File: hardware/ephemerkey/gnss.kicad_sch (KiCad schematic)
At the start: 12 parts

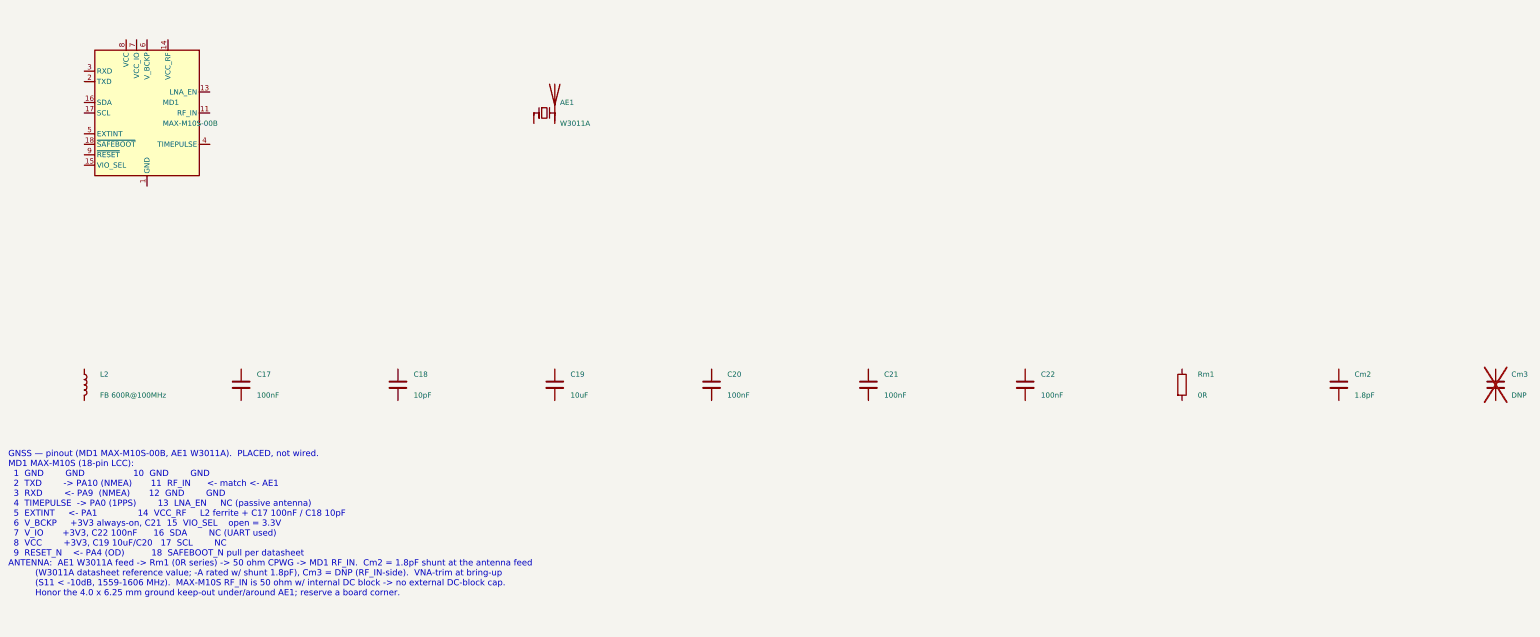
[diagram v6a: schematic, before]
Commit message: hardware: fix PSU load-share S/D, make all sheet notes monospace
The PSU wiring note specified Q1 (AO3401A load-share PMOS) as S=BAT+,
D=VSYS. A PMOS body diode conducts D->S, so that orientation points the
diode VSYS -> BAT+: with USB attached VSYS sits ~4.7V (VBUS - D3) against
a 3.0-4.2V cell, forward-biasing it and dumping uncontrolled current into
the battery, bypassing the MCP73831 charger entirely.

Correct assignment is D=BAT+, S=VSYS, so the body diode points BAT+ ->
VSYS: the battery always reaches the load, and USB can never back-feed
the cell. Q1 was placed but never wired (all three pins are unconnected
in the netlist), so this is a spec fix ahead of wiring, not a board
change. The lock's Q3 is a high-side switch and deliberately uses the
opposite S/D assignment; the note now says so, to stop the two being
"reconciled" by pattern-matching.

Also relaid the PSU note as a two-column table and gave every sheet note
the Courier New face the generator already emits (kschgen NOTE_FONT, added
in 43a6067). The sheets predate that commit, so their notes rendered in
KiCad's variable-width stroke font and the space-padded pin tables did not
line up. Font only on the other six notes -- text is untouched.

Verified: kicad-cli netlists for both boards are byte-identical before and
after (ephemerkey 259 nodes, lock 131 nodes) once the export timestamp is
excluded; no non-font lines changed in any sheet; all sheets re-rendered
and the notes fit inside the page frame.

The four ephemerkey sheets also carry pre-existing eeschema reformatting
(expanded lib_symbols) that was already in the working tree.

Co-Authored-By: Claude Opus 4.8 (1M context) <noreply@anthropic.com>
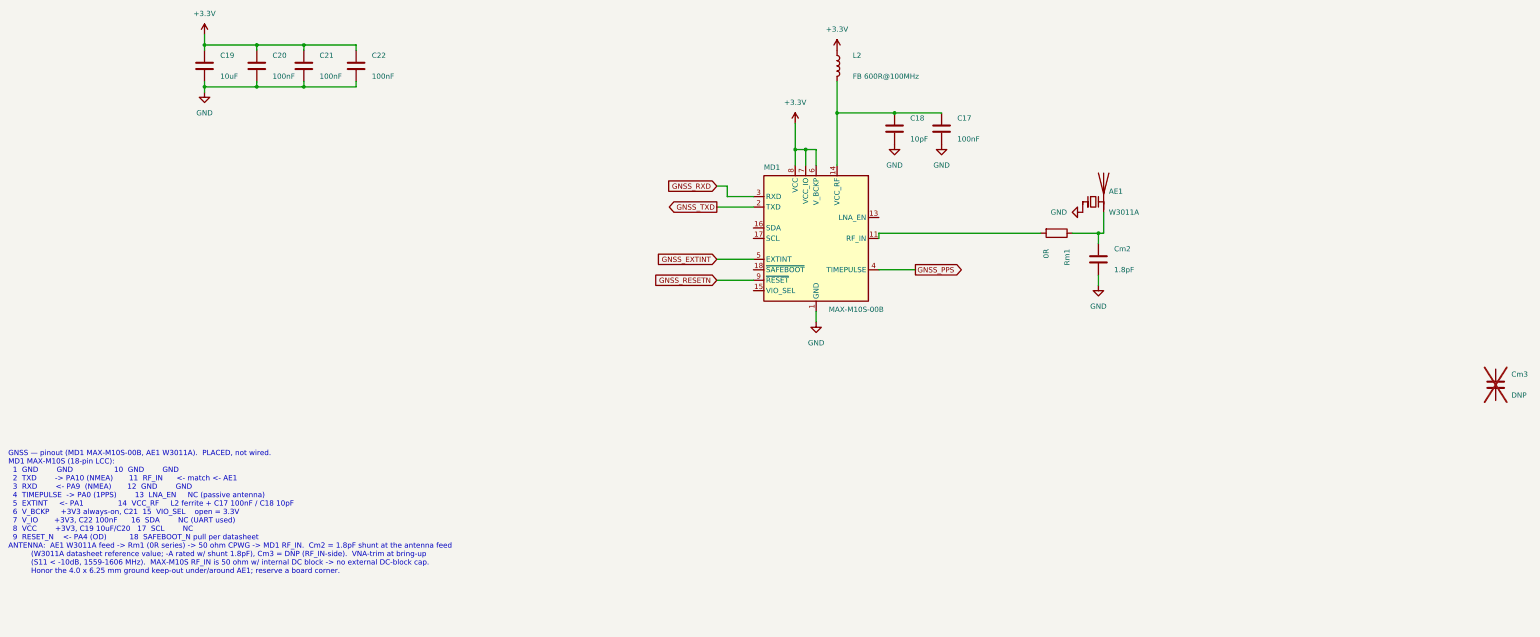
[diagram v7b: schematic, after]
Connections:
- net +3.3V: now reaches C19.1
- net +3.3V: now also C20.1, C21.1, C22.1, L2.1, MD1.6 (V_BCKP), MD1.7 (VCC_IO), MD1.8 (VCC)
- net GND: now reaches C19.2
- net GND: now also AE1.1 (FEED), C17.2, C18.2, C20.2, C21.2, C22.2, Cm2.2, MD1.1 (GND), MD1.10 (GND), MD1.12 (GND)
- net at C18.1: now also C17.1, L2.2, MD1.14 (VCC_RF)
- net at Cm2.1: now also AE1.2 (PCB_Trace), Rm1.1
- net at MD1.11 (RF_IN): now also Rm1.2
- net GNSS_TXD: now reaches MD1.2 (TXD)
- net GNSS_RXD: now reaches MD1.3 (RXD)
- net GNSS_PPS: now reaches MD1.4 (TIMEPULSE)
- net GNSS_EXTINT: now reaches MD1.5 (EXTINT)
- net GNSS_RESETN: now reaches MD1.9 (~{RESET})
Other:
- moved on the sheet: AE1, C17, C18, C19, C20, C21, C22, Cm2, L2, MD1, Rm1

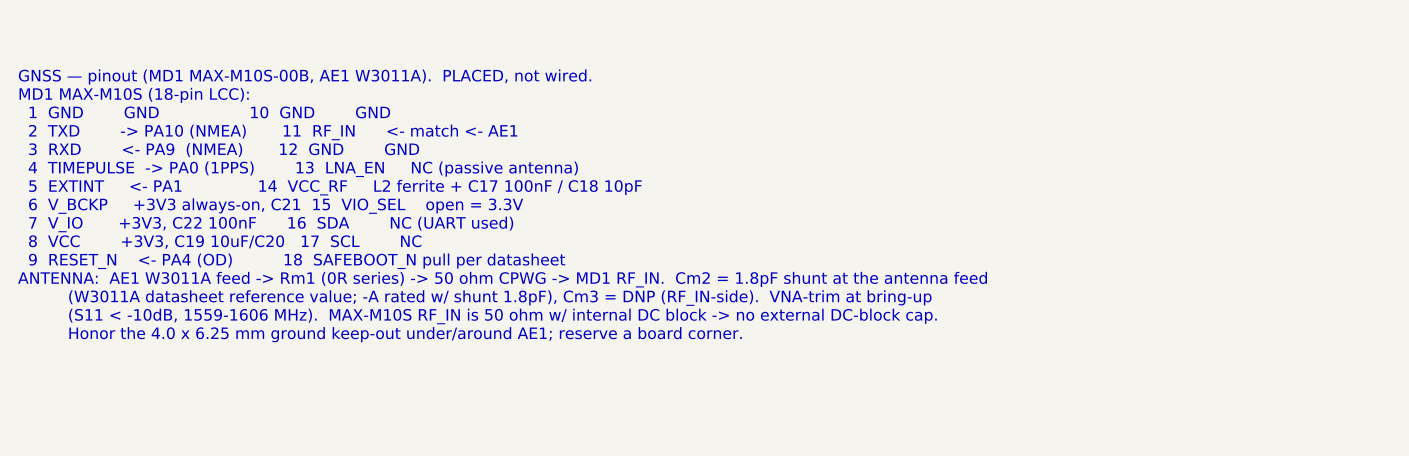
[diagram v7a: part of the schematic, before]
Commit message: hardware: GPS antenna contingency — capacitor-select U.FL connector
RF_IN now taps two series positions: Rm1 (0R -> on-board W3011A chip antenna,
default) and Cs1 (DNP -> J6, a Hirose U.FL-R-SMT-1). Populate exactly one; to
run an external antenna, DNP Rm1, fit Cs1 (0R or DC-block cap) and cable in via
the U.FL. Passive external patch needs no bias; an active antenna needs a
bias-tee (not fitted — noted in the sheet + DESIGN.md).

J6 uses the generic 2-pin symbol (center/shield) on the Connector_Coaxial U.FL
land; Cs1 is a DNP 0402. schgen.py is the source of truth; J6/Cs1 spliced into
the wired gnss sheet as PLACED (unwired) — wire them in eeschema (RF_IN -> Cs1
-> J6.1, J6.2 -> GND). make check-ephemerkey: 101 components, no dup refs,
structure sound.

Co-Authored-By: Claude Opus 4.8 <noreply@anthropic.com>
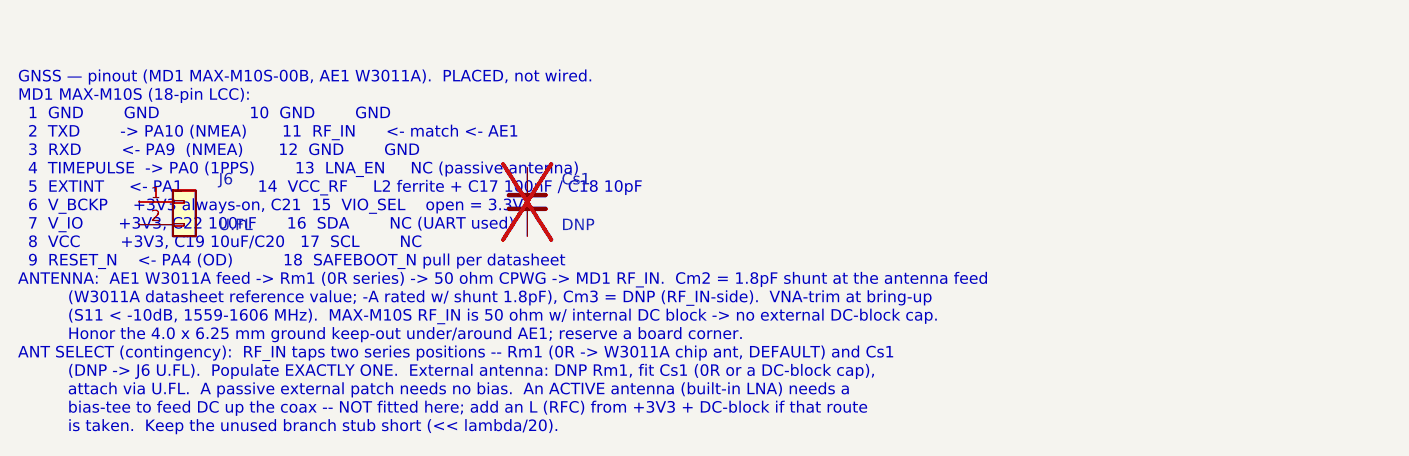
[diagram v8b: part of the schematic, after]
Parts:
- added Cs1: DNP, Capacitor_SMD:C_0402_1005Metric, symbol Device:C
- added J6: U.FL, Connector_Coaxial:U.FL_Hirose_U.FL-R-SMT-1_Vertical, symbol Connector_Generic:Conn_01x02
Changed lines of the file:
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@@
 		(company "EphemerKey Authors")
 	)
-	(text "GNSS — pinout (MD1 MAX-M10S-00B, AE1 W3011A).  PLACED, not wired.\nMD1 MAX-M10S (18-pin LCC):\n  1  GND        GND                  10  GND        GND\n  2  TXD        -> PA10 (NMEA)       11  RF_IN      <- match <- AE1\n  3  RXD        <- PA9  (NMEA)       12  GND        GND\n  4  TIMEPULSE  -> PA0 (1PPS)        13  LNA_EN     NC (passive antenna)\n  5  EXTINT     <- PA1               14  VCC_RF     L2 ferrite + C17 100nF / C18 10pF\n  6  V_BCKP     +3V3 always-on, C21  15  VIO_SEL    open = 3.3V\n  7  V_IO       +3V3, C22 100nF      16  SDA        NC (UART used)\n  8  VCC        +3V3, C19 10uF/C20   17  SCL        NC\n  9  RESET_N    <- PA4 (OD)          18  SAFEBOOT_N pull per datasheet\nANTENNA:  AE1 W3011A feed -> Rm1 (0R series) -> 50 ohm CPWG -> MD1 RF_IN.  Cm2 = 1.8pF shunt at the antenna feed\n          (W3011A datasheet reference value; -A rated w/ shunt 1.8pF), Cm3 = DNP (RF_IN-side).  VNA-trim at bring-up\n          (S11 < -10dB, 1559-1606 MHz).  MAX-M10S RF_IN is 50 ohm w/ internal DC block -> no external DC-block cap.\n          Honor the 4.0 x 6.25 mm ground keep-out under/around AE1; reserve a board corner."
+	(text "GNSS — pinout (MD1 MAX-M10S-00B, AE1 W3011A).  PLACED, not wired.\nMD1 MAX-M10S (18-pin LCC):\n  1  GND        GND                  10  GND        GND\n  2  TXD        -> PA10 (NMEA)       11  RF_IN      <- match <- AE1\n  3  RXD        <- PA9  (NMEA)       12  GND        GND\n  4  TIMEPULSE  -> PA0 (1PPS)        13  LNA_EN     NC (passive antenna)\n  5  EXTINT     <- PA1               14  VCC_RF     L2 ferrite + C17 100nF / C18 10pF\n  6  V_BCKP     +3V3 always-on, C21  15  VIO_SEL    open = 3.3V\n  7  V_IO       +3V3, C22 100nF      16  SDA        NC (UART used)\n  8  VCC        +3V3, C19 10uF/C20   17  SCL        NC\n  9  RESET_N    <- PA4 (OD)          18  SAFEBOOT_N pull per datasheet\nANTENNA:  AE1 W3011A feed -> Rm1 (0R series) -> 50 ohm CPWG -> MD1 RF_IN.  Cm2 = 1.8pF shunt at the antenna feed\n          (W3011A datasheet reference value; -A rated w/ shunt 1.8pF), Cm3 = DNP (RF_IN-side).  VNA-trim at bring-up\n          (S11 < -10dB, 1559-1606 MHz).  MAX-M10S RF_IN is 50 ohm w/ internal DC block -> no external DC-block cap.\n          Honor the 4.0 x 6.25 mm ground keep-out under/around AE1; reserve a board corner.\nANT SELECT (contingency):  RF_IN taps two series positions -- Rm1 (0R -> W3011A chip ant, DEFAULT) and Cs1\n          (DNP -> J6 U.FL).  Populate EXACTLY ONE.  External antenna: DNP Rm1, fit Cs1 (0R or a DC-block cap),\n          attach via U.FL.  A passive external patch needs no bias.  An ACTIVE antenna (built-in LNA) needs a\n          bias-tee to feed DC up the coax -- NOT fitted here; add an L (RFC) from +3V3 + DC-block if that route\n          is taken.  Keep the unused branch stub short (<< lambda/20)."
 		(exclude_from_sim no)
 		(at 12 137.92 0)
@@
 					(unit 1)
 				)
+			)
+		)
+	)
+	(symbol
+		(lib_id "Connector_Generic:Conn_01x02")
+		(at 30.4800 152.4000 0)
+		(unit 1)
+		(exclude_from_sim no)
+		(in_bom yes)
+		(on_board yes)
+		(dnp no)
+		(property "Reference" "J6"
+			(at 34.2900 149.8600 0)
+			(effects (font (size 1.27 1.27)) (justify left))
+		)
+		(property "Value" "U.FL"
+			(at 34.2900 154.9400 0)
+			(effects (font (size 1.27 1.27)) (justify left))
+		)
+		(property "Footprint" "Connector_Coaxial:U.FL_Hirose_U.FL-R-SMT-1_Vertical"
+			(at 30.4800 152.4000 0)
+			(effects (font (size 1.27 1.27))) (hide yes)
+		)
+		(property "Datasheet" "~"
+			(at 30.4800 152.4000 0)
+			(effects (font (size 1.27 1.27))) (hide yes)
+		)
+		(property "LCSC" "C88373"
+			(at 30.4800 152.4000 0)
+			(effects (font (size 1.27 1.27))) (hide yes)
+		)
+		(property "MPN" "U.FL-R-SMT-1(10)"
+			(at 30.4800 152.4000 0)
+			(effects (font (size 1.27 1.27))) (hide yes)
+		)
+		(property "Manufacturer" "Hirose"
+			(at 30.4800 152.4000 0)
+			(effects (font (size 1.27 1.27))) (hide yes)
+		)
+		(pin "1")
+		(pin "2")
+		(instances
+			(project "ephemerkey"
+				(path "/ec65bc99-660e-415e-984b-47a2d6256a80/29c883c7-b979-475a-b755-896ca253f844"
+					(reference "J6")
+					(unit 1)
+				)
+			)
+		)
+	)
+	(symbol
+		(lib_id "Device:C")
+		(at 68.5800 152.4000 0)
+		(unit 1)
+		(exclude_from_sim no)
+		(in_bom yes)
+		(on_board yes)
+		(dnp yes)
+		(property "Reference" "Cs1"
+			(at 72.3900 149.8600 0)
+			(effects (font (size 1.27 1.27)) (justify left))
+		)
+		(property "Value" "DNP"
+			(at 72.3900 154.9400 0)
+			(effects (font (size 1.27 1.27)) (justify left))
+		)
+		(property "Footprint" "Capacitor_SMD:C_0402_1005Metric"
+			(at 68.5800 152.4000 0)
+			(effects (font (size 1.27 1.27))) (hide yes)
+		)
+		(property "Datasheet" "~"
+			(at 68.5800 152.4000 0)
+			(effects (font (size 1.27 1.27))) (hide yes)
+		)
+		(pin "1")
+		(pin "2")
+		(instances
+			(project "ephemerkey"
+				(path "/ec65bc99-660e-415e-984b-47a2d6256a80/29c883c7-b979-475a-b755-896ca253f844"
+					(reference "Cs1")
+					(unit 1)
+				)
